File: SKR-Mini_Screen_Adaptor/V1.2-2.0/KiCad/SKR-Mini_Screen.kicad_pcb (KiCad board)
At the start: 2 copper layers, 22.9 x 43.2 mm, 6 parts, among them J1 Board_EXP1, J2 Board_SPI, J3 Screen_EXP1, J4 Screen_EXP2

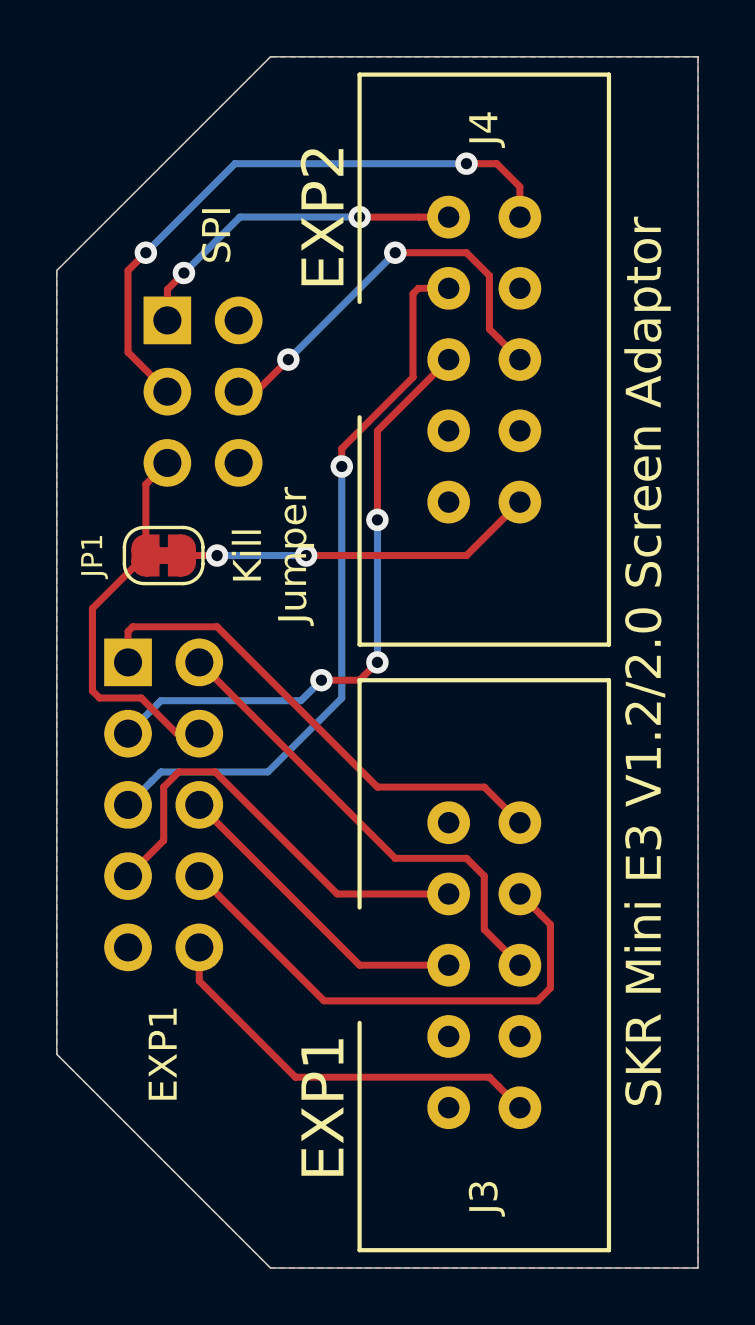
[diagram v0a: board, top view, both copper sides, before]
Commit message: Update header pin spacing
 - Update header pin spacing from 0.75 to 1mm to aid in fit for some shrouded headers
 - Update project to KiCad 6.0
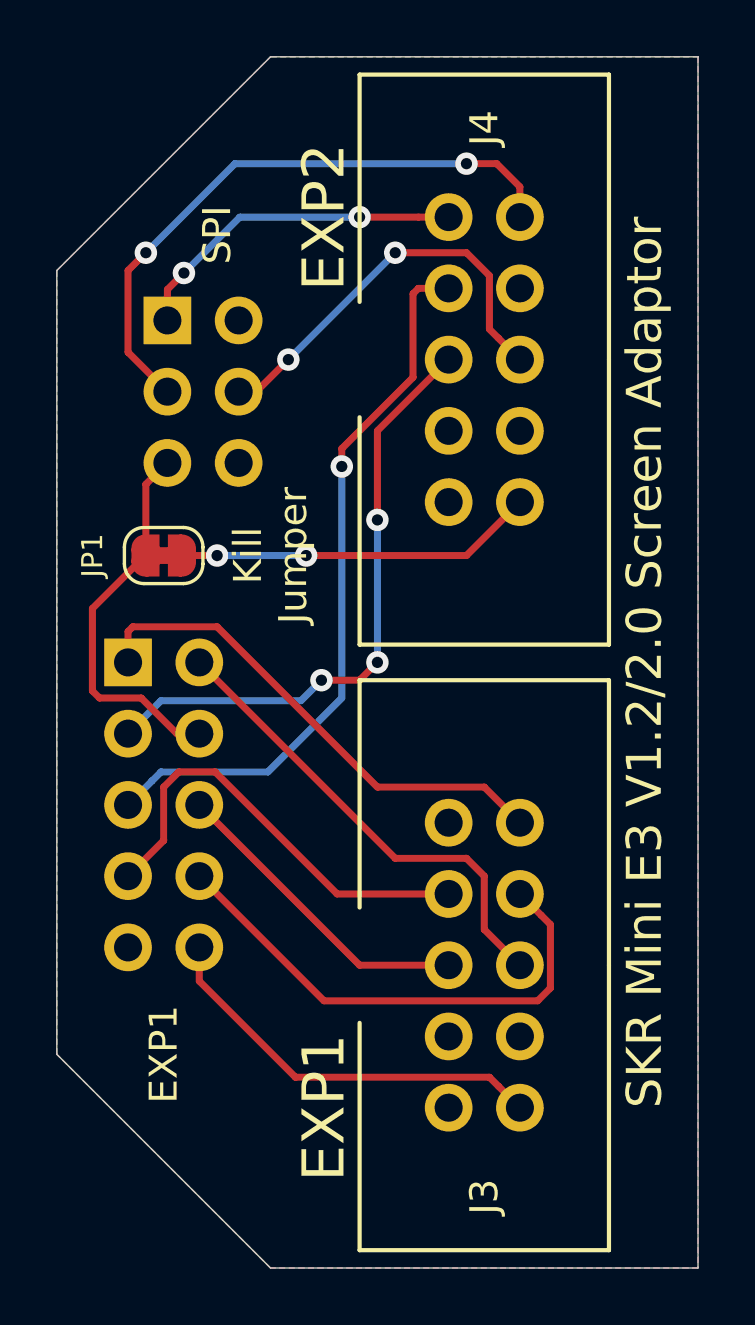
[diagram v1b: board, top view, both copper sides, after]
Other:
- net class Default removed

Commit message: Revision Update notes
Added revision update notes to Readme and indicator to the PCB
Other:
- board text added: "T. Abraham Rev: B"
- board text removed: "T. Abraham RevA"
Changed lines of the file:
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@@
     (effects (font (size 1 1) (thickness 0.2)) (justify mirror))
   )
-  (gr_text "T. Abraham RevA" (at 132.715 106.68 90) (layer "B.SilkS")
+  (gr_text "T. Abraham Rev: B" (at 132.715 106.68 90) (layer "B.SilkS")
     (effects (font (size 1 1) (thickness 0.2)) (justify mirror))
   )
@@
   (zone (net 1) (net_name "/+5V") (layer "F.Cu") (hatch edge 0.508)
     (connect_pads (clearance 0.508))
-    (min_thickness 0.254)
+    (min_thickness 0.254) (filled_areas_thickness no)
     (fill yes (thermal_gap 0.508) (thermal_bridge_width 0.508))
     (polygon
@@
   (zone (net 2) (net_name "/GND") (layer "B.Cu") (hatch edge 0.508)
     (connect_pads (clearance 0.508))
-    (min_thickness 0.254)
+    (min_thickness 0.254) (filled_areas_thickness no)
     (fill yes (thermal_gap 0.508) (thermal_bridge_width 0.508))
     (polygon
